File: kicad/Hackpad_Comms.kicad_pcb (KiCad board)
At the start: 2 copper layers, 86 x 85 mm, 27 parts, among them SW1 SW_Push, SW10 SW_Push, SW11 SW_Push, SW12 SW_Push, SW14 RotaryEncoder, SW2 SW_Push, SW3 SW_Push, SW4 SW_Push, SW5 SW_Push, SW6 SW_Push, SW7 SW_Push, SW8 SW_Push, SW9 SW_Push, U1 XIAO-RP2040-DIP

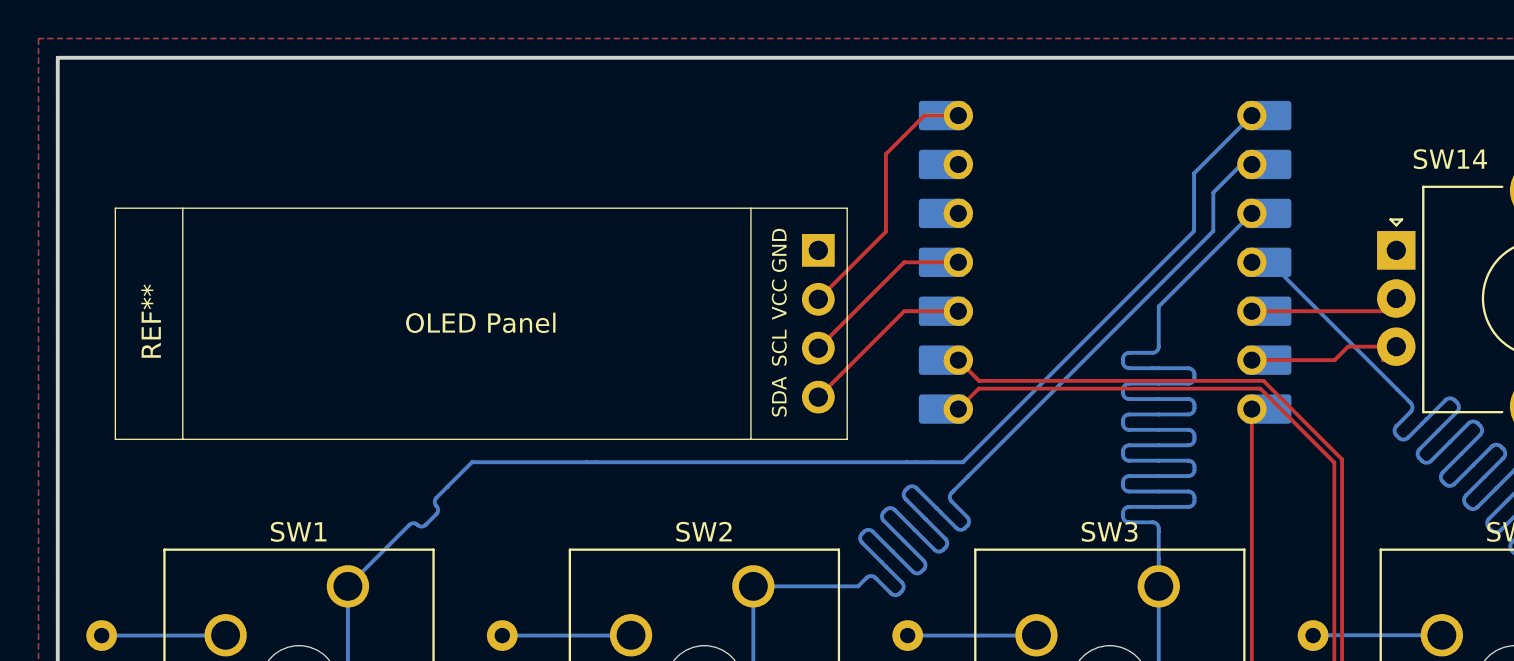
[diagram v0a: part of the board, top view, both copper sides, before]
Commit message: PCB Rev2; Add more images; Basic HID firmware prototype
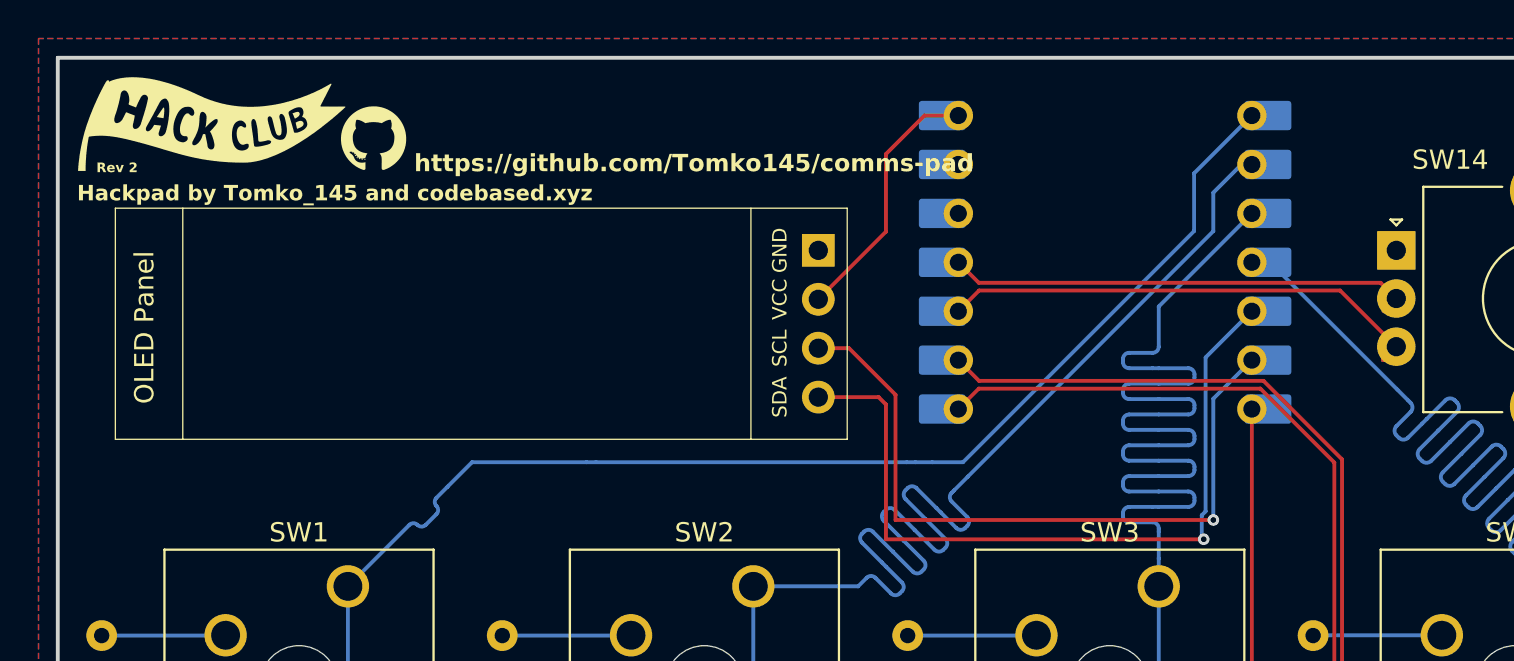
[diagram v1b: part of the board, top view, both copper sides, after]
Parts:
- renumbered REF** to OLED
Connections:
- OLED pad 3: unconnected-(U1-GPIO3/MOSI-Pad11) -> Net-(U1-GPIO7/SCL)
- OLED pad 4: unconnected-(U1-GPIO4/MISO-Pad10) -> Net-(U1-GPIO6/SDA)
- SW14 pad B: Net-(U1-GPIO7/SCL) -> unconnected-(U1-GPIO4/MISO-Pad10)
- SW14 pad C: Net-(U1-GPIO6/SDA) -> unconnected-(U1-GPIO3/MOSI-Pad11)
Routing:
- net Net-(U1-GPIO6/SDA): track 8.71 -> 40.1 mm, vias 0 -> 1
- net Net-(U1-GPIO7/SCL): track 9.77 -> 37.1 mm, vias 0 -> 1
- net unconnected-(U1-GPIO4/MISO-Pad10): track 9.12 -> 26.9 mm
- net unconnected-(U1-GPIO3/MOSI-Pad11): track 9.12 -> 25.4 mm
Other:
- board text added: "Hackpad by Tomko_145 and codebased.xyz"
- board text added: "Rev 2"
- board text added: "https://github.com/Tomko145/comms-pad"
